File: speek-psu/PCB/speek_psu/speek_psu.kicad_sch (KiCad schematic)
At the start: 21 parts, among them J1 Conn_01x02, J2 Conn_01x02, J3 Conn_01x02, J4 Conn_01x02, J5 Conn_01x02, J6 Conn_01x02, J7 Conn_01x02, J8 Conn_01x02, J9 Conn_01x02, U1 10k, U2 CH224K

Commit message: JST and antenna
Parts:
- added D1, D2: PMEG060V100EPDZ, easyeda2kicad:SOT1289_L5.8-W4.4-LS6.5-RD, symbol lcsc:PMEG060V100EPDZ
- added U3: 25PX4700MEFC16X25, easyeda2kicad:CAP-TH_BD16.0-P7.50-D1.2-FD, symbol lcsc:25PX4700MEFC16X25
- added U4: XT60, easyeda2kicad:CONN-TH_XT60, symbol lcsc:XT60
- J1, J2, J3, J4, J5, J6, J7, J8: footprint Connector_JST:JST_EH_S2B-EH_1x02_P2.50mm_Horizontal -> Connector_JST:JST_VH_B2P-VH-B_1x02_P3.96mm_Vertical
- J9: now not fitted
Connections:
- net GND: now also U3.2, U4.1 (-)
- net VBUS: now also D2.1 (A), D2.2 (A); no longer J1.2 (Pin_2), J2.2 (Pin_2), J3.2 (Pin_2), J4.2 (Pin_2), J5.2 (Pin_2), J6.2 (Pin_2), J7.2 (Pin_2), J8.2 (Pin_2), J9.2 (Pin_2)
- new net: D1.1 (A), D1.2 (A), U4.2 (+)
- new net _VOUT: D1.3 (K), D2.3 (K), J1.2 (Pin_2), J2.2 (Pin_2), J3.2 (Pin_2), J4.2 (Pin_2), J5.2 (Pin_2), J6.2 (Pin_2), J7.2 (Pin_2), J8.2 (Pin_2), J9.2 (Pin_2), U3.1

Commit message: [Speek Amp] Schematic rework
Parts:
- removed U3: 25PX4700MEFC16X25, easyeda2kicad:CAP-TH_BD16.0-P7.50-D1.2-FD, symbol lcsc:25PX4700MEFC16X25
- added U5: 50PX4700MEFC18X40, easyeda2kicad:CAP-TH_BD18.0-P7.50-D0.8-FD, symbol lcsc:50PX4700MEFC18X40
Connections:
- net GND: now also U5.2
- net _VOUT: now also U5.1

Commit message: connectors
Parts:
- added U3, U6, U7, U8: (no value), easyeda2kicad:CONN-TH_DB301V-3.5-2P-GN, symbol lcsc:DB301V-3.5-2P-GN
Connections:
- net GND: now also U3.1, U6.1, U7.1, U8.1
- net _VOUT: now also U3.2, U6.2, U7.2, U8.2

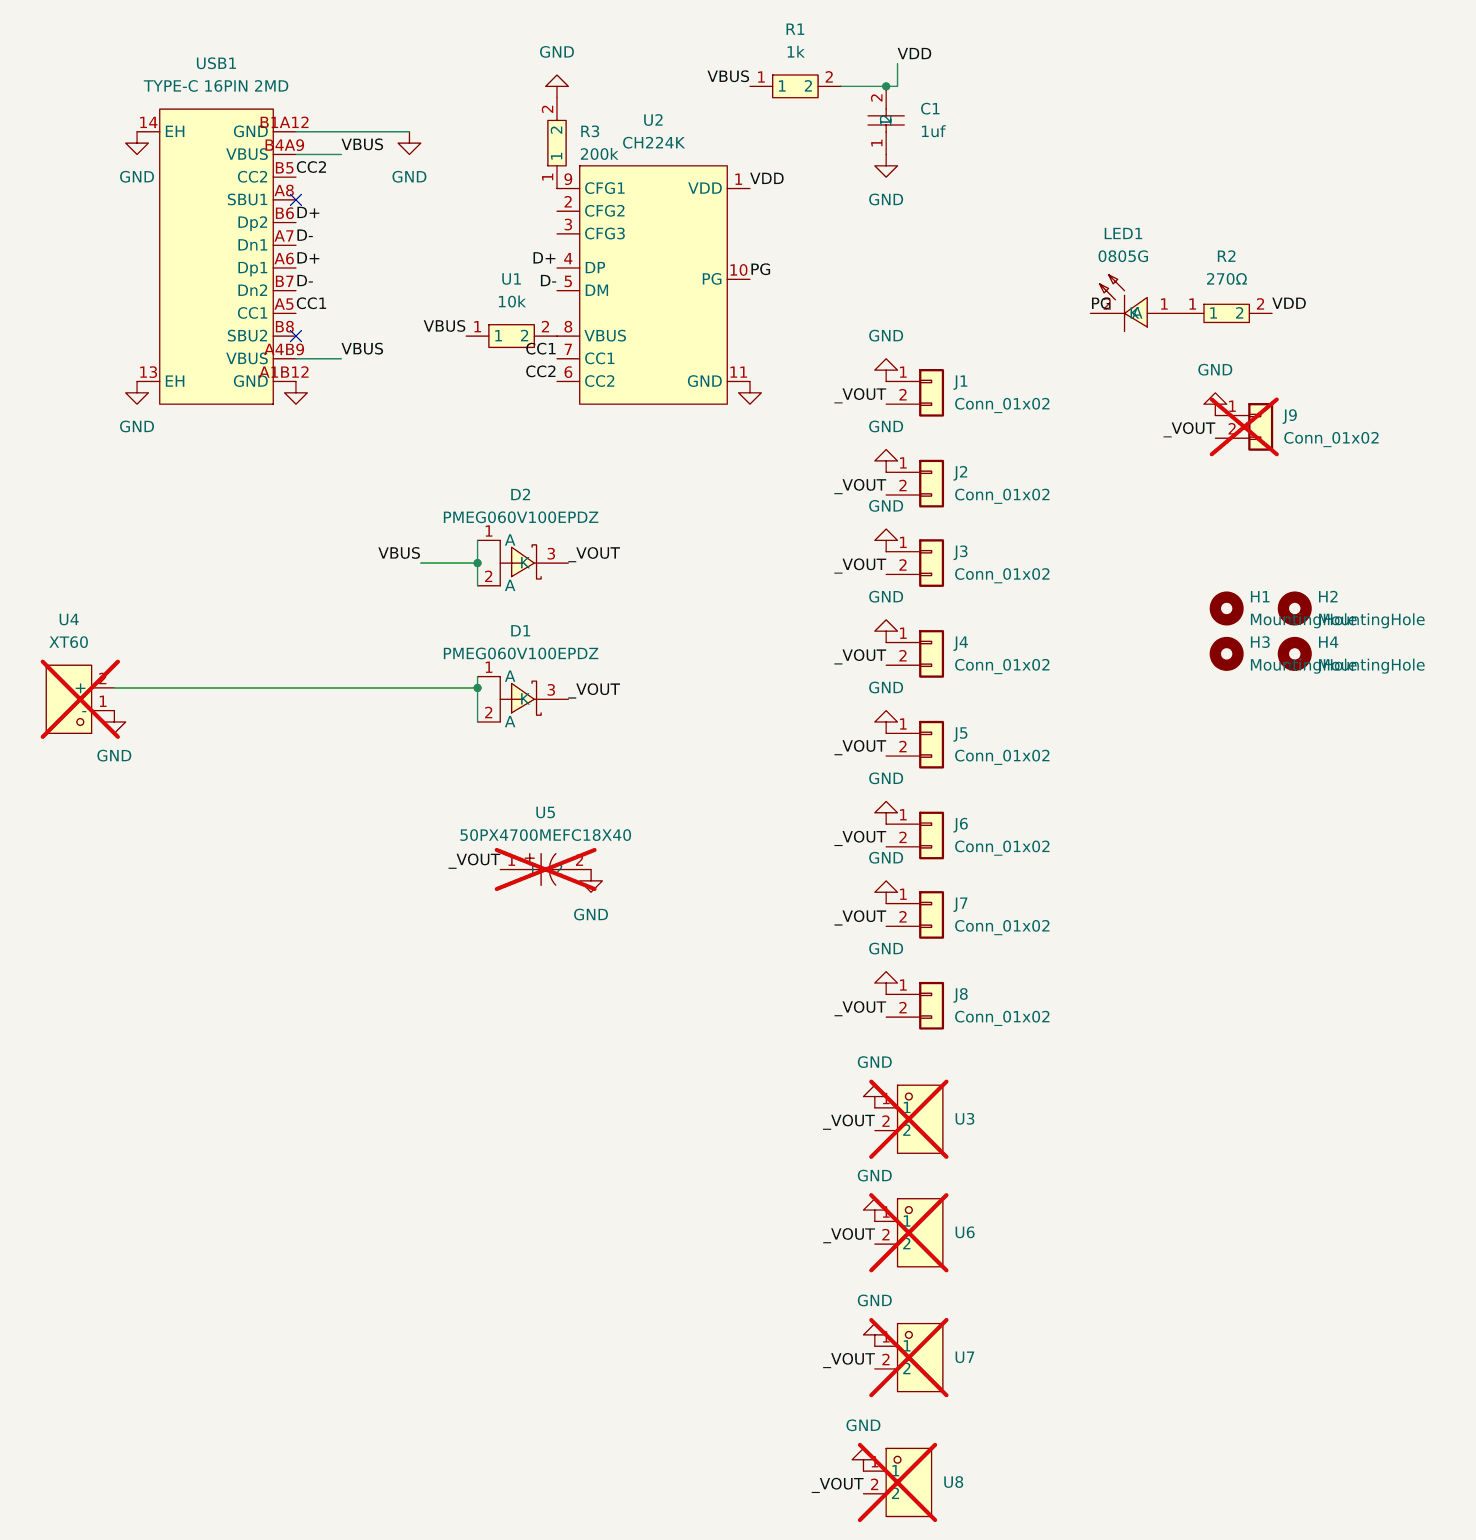
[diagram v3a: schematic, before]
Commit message: Speek PSU no longer requires PCBA !!
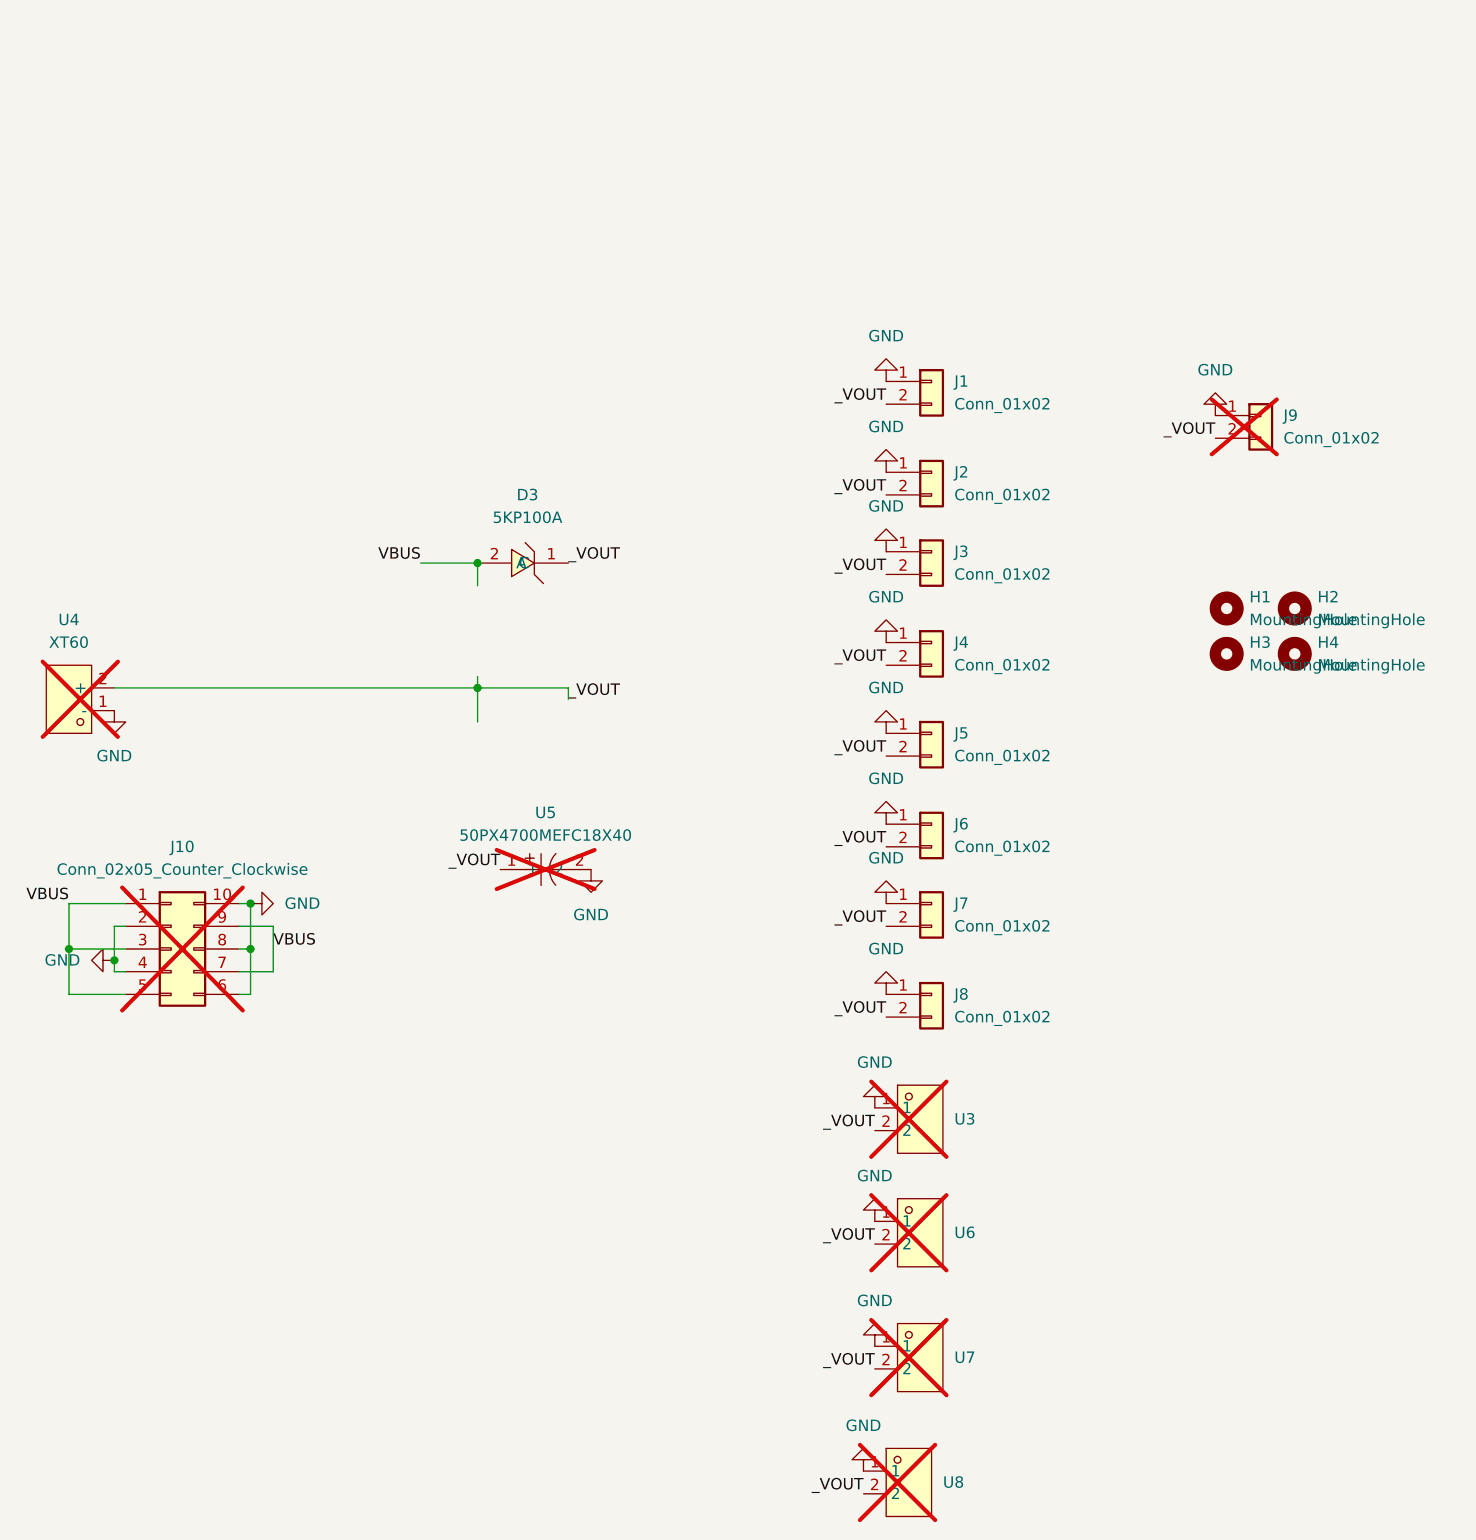
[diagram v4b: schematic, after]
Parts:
- removed C1: 1uf, easyeda2kicad:C0603, symbol lcsc:CL10B105KA8NNNC
- removed D1, D2: PMEG060V100EPDZ, easyeda2kicad:SOT1289_L5.8-W4.4-LS6.5-RD, symbol lcsc:PMEG060V100EPDZ
- removed LED1: 0805G, easyeda2kicad:LED0805-R-RD, symbol lcsc:0805G
- removed R1: 1k, easyeda2kicad:R2010, symbol lcsc:FRC2010F1001TS
- removed R2: 270Ω, easyeda2kicad:R0603, symbol lcsc:0603WAF2700T5E
- removed R3: 200k, easyeda2kicad:R0402, symbol easyeda2kicad:0402WGF2003TCE
- removed U1: 10k, easyeda2kicad:R0805, symbol lcsc:FRC0805F1002TS
- removed U2: CH224K, easyeda2kicad:ESSOP-10_L4.9-W3.9-P1.0-LS6.0-TL-EP, symbol lcsc:CH224K
- removed USB1: TYPE-C 16PIN 2MD, easyeda2kicad:USB-C-SMD_TYPE-C-16PIN-2MD-073, symbol lcsc:TYPE-C16PIN2MD
- added D3: 5KP100A, easyeda2kicad:DIO-TH_BD8.8-L8.8-P12.8-D1.6-RD, symbol lcsc:5KP100A
- added J10: Conn_02x05_Counter_Clockwise, Connector_PinHeader_2.54mm:PinHeader_2x05_P2.54mm_Horizontal, symbol Connector_Generic:Conn_02x05_Counter_Clockwise
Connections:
- net GND: now also J10.10 (Pin_10), J10.2 (Pin_2), J10.4 (Pin_4), J10.6 (Pin_6), J10.8 (Pin_8)
- net VBUS: now also D3.2 (A), J10.1 (Pin_1), J10.3 (Pin_3), J10.5 (Pin_5), J10.7 (Pin_7), J10.9 (Pin_9)
- net _VOUT: now also U4.2 (+), D3.1 (C)
- no-connect marks 2 -> 0

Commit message: dnp d3
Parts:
- D3: now not fitted
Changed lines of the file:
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@@
 		(on_board yes)
 		(in_pos_files yes)
-		(dnp no)
+		(dnp yes)
 		(fields_autoplaced yes)
 		(property "Reference" "D3"
